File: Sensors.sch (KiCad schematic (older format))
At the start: 68 parts, among them CON1 CONSOLE, IC1 ATMEGA328P, P1 CONN_01X08, P10 GPIO, P11 I2C, P12 96B-GPIO, P13 96B-I2C0, P14 GPIO, P15 GPIO, P16 GPIO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

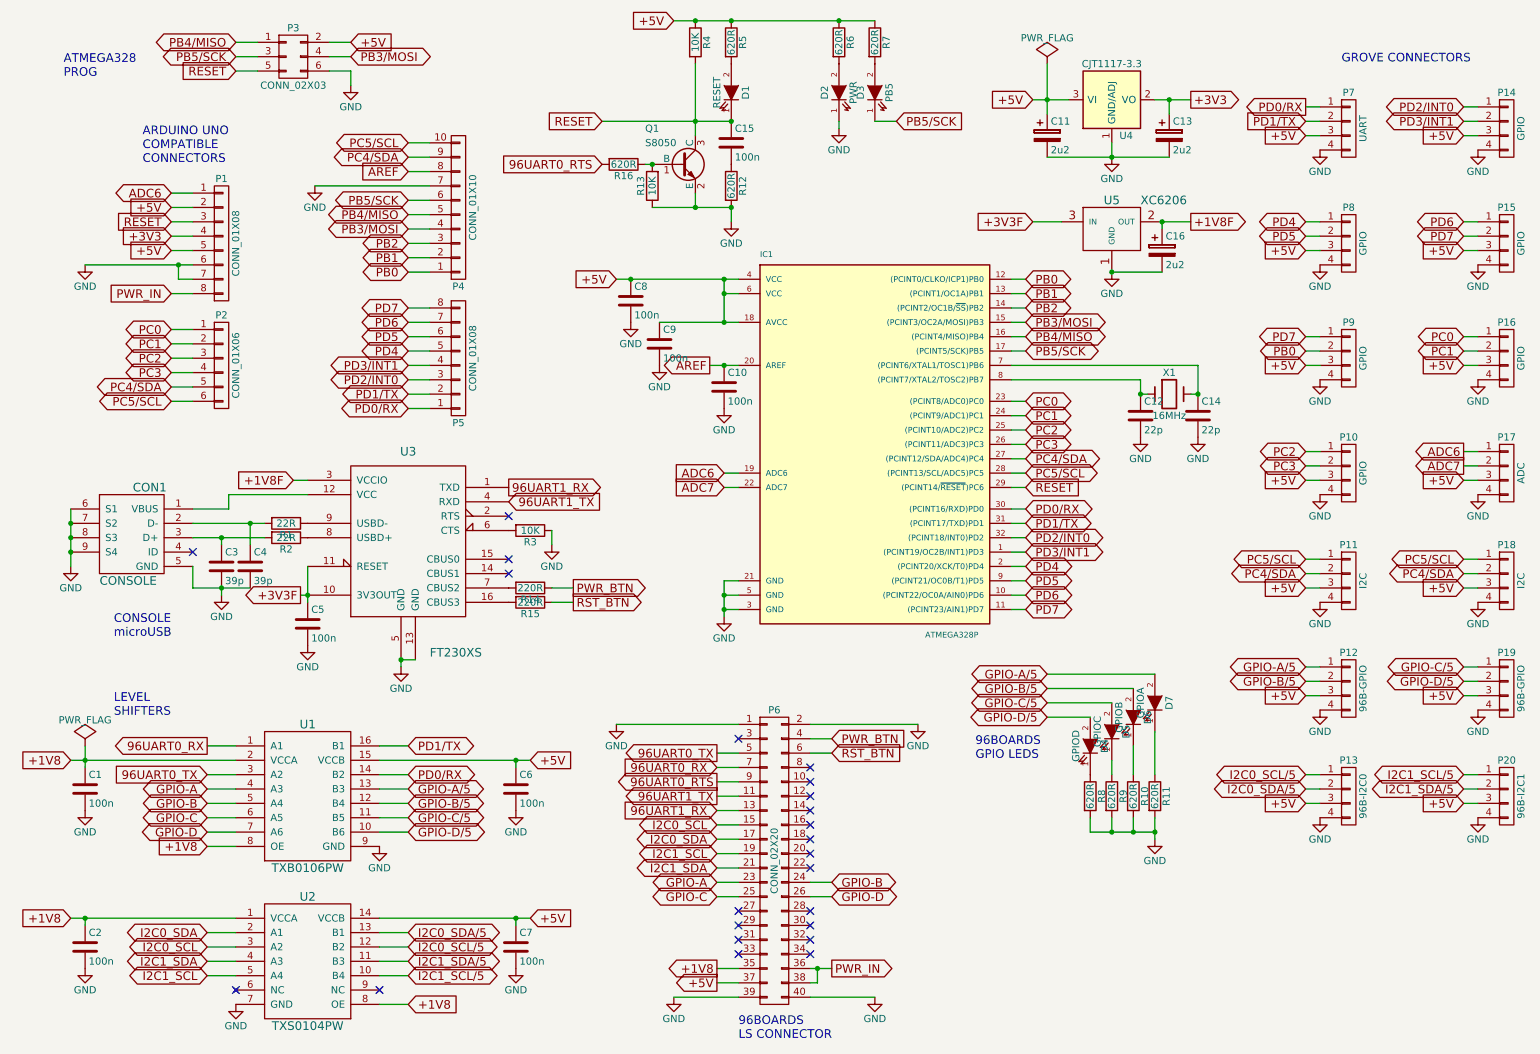
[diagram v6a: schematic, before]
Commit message: Rewire PB5 LED to drive high to light and use a 1K resistor
The first rev had the LED tied to +5V, and PB5 needed to pull it low to
light. This doesn't play well with USBTinyISP because it puts too much
load on the line for the programmer to actually program the Arduino, and
it is opposite to the way the led is wired on every other Arduino. Fix
it to be consistent with the rest of the Arduino world.

Signed-off-by: Grant Likely <grant.likely@linaro.org>
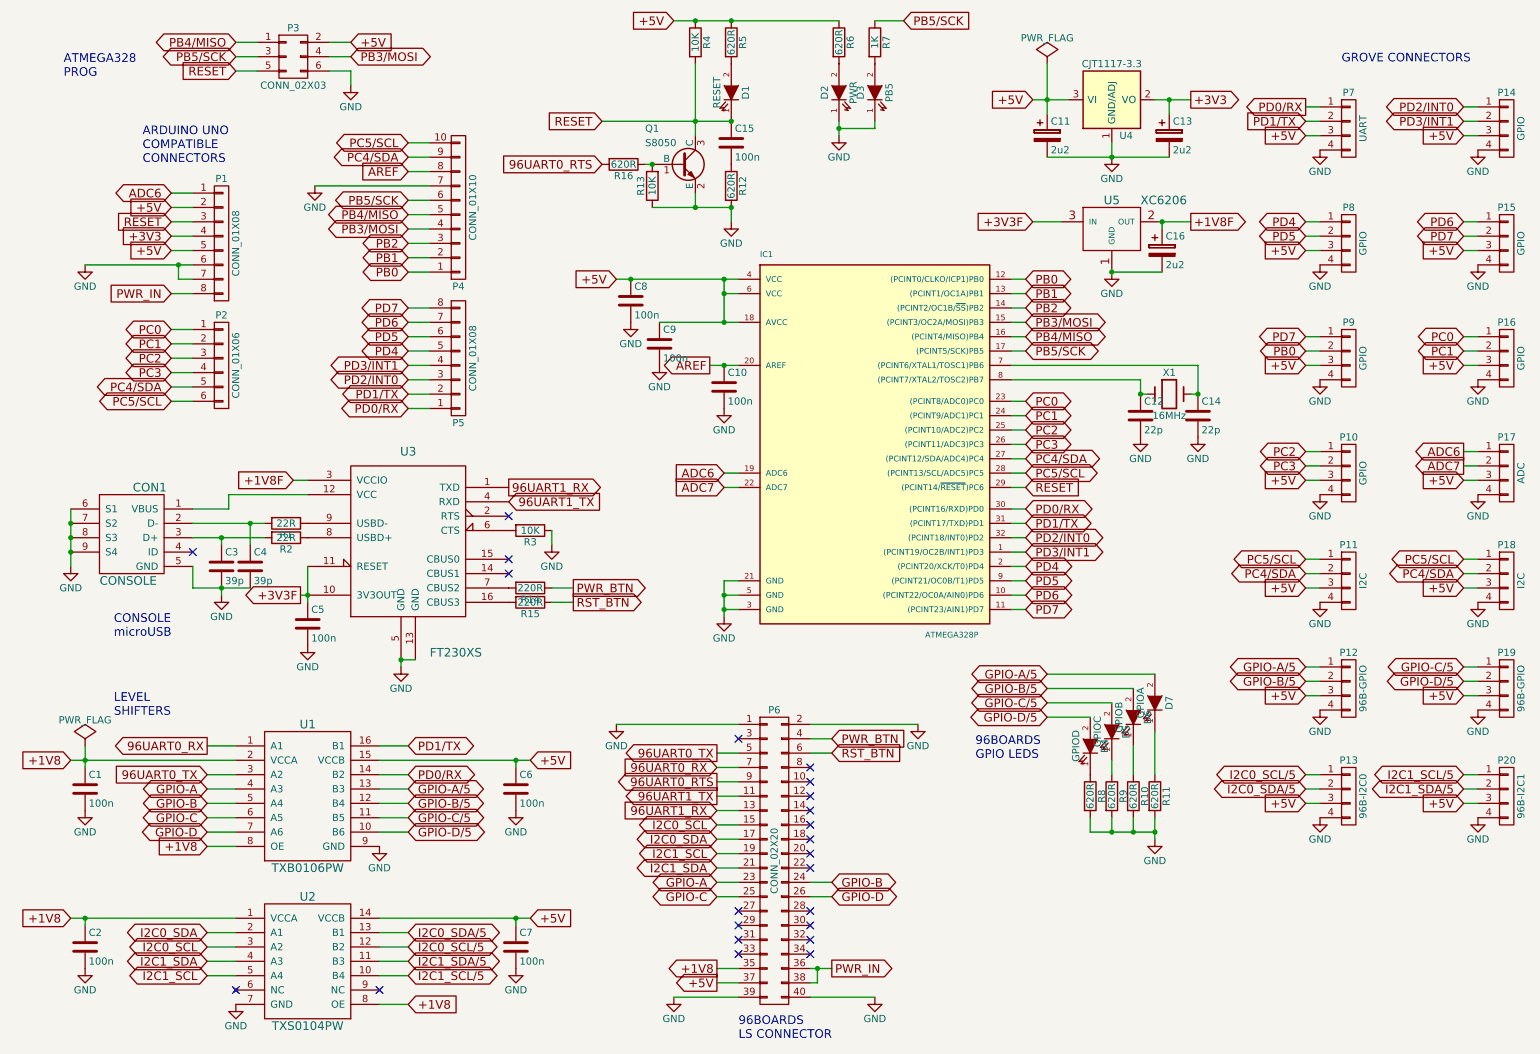
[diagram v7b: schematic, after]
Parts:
- R7: value 620R -> 1K
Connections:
- net +5V: no longer R7.1
- net GND: now also D3.1 (K)
- net PB5/SCK: now also R7.1; no longer D3.1 (K)
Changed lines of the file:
@@
 L GND #PWR030
 U 1 1 55BFA7BD
-P 6250 1350
-F 0 "#PWR030" H 6250 1100 50  0001 C CNN
-F 1 "GND" H 6250 1200 50  0000 C CNN
-F 2 "" H 6250 1350 60  0000 C CNN
-F 3 "" H 6250 1350 60  0000 C CNN
-	1    6250 1350
+P 6250 1400
+F 0 "#PWR030" H 6250 1150 50  0001 C CNN
+F 1 "GND" H 6250 1250 50  0000 C CNN
+F 2 "" H 6250 1400 60  0000 C CNN
+F 3 "" H 6250 1400 60  0000 C CNN
+	1    6250 1400
 	1    0    0    -1
 $EndComp
@@
 P 6500 750
 F 0 "R7" V 6580 750 50  0000 C CNN
-F 1 "620R" V 6500 750 50  0000 C CNN
+F 1 "1K" V 6500 750 50  0000 C CNN
 F 2 "Sensors:R_0603_Seeed" V 6430 750 30  0001 C CNN
 F 3 "" H 6500 750 30  0000 C CNN
@@
 	0    -1   -1   0
 $EndComp
-Text GLabel 6650 1300 2    60   Input ~ 0
+Text GLabel 6700 600  2    60   Input ~ 0
 PB5/SCK
 Text GLabel 5400 6000 0    60   Output ~ 0
@@
 	1750 3250 1600 3250
 Wire Wire Line
-	1000 2300 1650 2300
-Wire Wire Line
-	1650 2300 1750 2300
+	1000 2300 1750 2300
 Wire Wire Line
 	1750 2400 1650 2400
@@
 	7450 2900 7550 2900
 Wire Wire Line
-	4700 2400 4800 2400
-Wire Wire Line
-	4800 2400 5450 2400
-Wire Wire Line
-	5450 2400 5550 2400
+	4700 2400 5550 2400
 Wire Wire Line
 	5550 2500 5450 2500
 Wire Wire Line
-	5450 2400 5450 2500
-Wire Wire Line
-	5450 2500 5450 2700
+	5450 2400 5450 2700
 Connection ~ 5450 2400
 Connection ~ 4800 2400
 Wire Wire Line
-	5000 2700 5450 2700
-Wire Wire Line
-	5450 2700 5550 2700
-Wire Wire Line
-	5350 3000 5450 3000
-Wire Wire Line
-	5450 3000 5550 3000
+	5000 2700 5550 2700
+Wire Wire Line
+	5350 3000 5550 3000
 Wire Wire Line
 	7450 3000 8750 3000
@@
 	5550 4500 5450 4500
 Wire Wire Line
-	5450 4500 5450 4600
-Wire Wire Line
-	5450 4600 5450 4700
-Wire Wire Line
-	5450 4700 5450 4750
+	5450 4500 5450 4750
 Wire Wire Line
 	5450 4700 5550 4700
@@
 	5400 5800 5550 5800
 Wire Wire Line
-	8450 1150 8550 1150
-Wire Wire Line
-	8550 1150 8700 1150
-Wire Wire Line
-	7700 1550 8150 1550
-Wire Wire Line
-	8150 1550 8550 1550
+	8450 1150 8700 1150
+Wire Wire Line
+	7700 1550 8550 1550
 Wire Wire Line
 	8550 1250 8550 1150
@@
 Connection ~ 5500 600
 Wire Wire Line
-	4600 1300 5250 1300
-Wire Wire Line
-	5250 1300 5500 1300
+	4600 1300 5500 1300
 Connection ~ 5250 1300
 Connection ~ 5500 1300
 Wire Wire Line
-	5100 600  5250 600
-Wire Wire Line
-	5250 600  5500 600
-Wire Wire Line
-	5500 600  6250 600
-Wire Wire Line
-	6250 600  6500 600
+	5100 600  6250 600
 Wire Wire Line
 	1850 5650 2050 5650
 Wire Wire Line
-	900  5750 1000 5750
-Wire Wire Line
-	1000 5750 2050 5750
+	900  5750 2050 5750
 Connection ~ 1000 5750
 Wire Wire Line
-	1000 5650 1000 5750
-Wire Wire Line
-	1000 5750 1000 5800
+	1000 5650 1000 5800
 Wire Wire Line
 	3050 5650 3250 5650
 Wire Wire Line
-	3050 5750 4000 5750
-Wire Wire Line
-	4000 5750 4100 5750
+	3050 5750 4100 5750
 Connection ~ 4000 5750
 Wire Wire Line
@@
 	3250 7450 3050 7450
 Wire Wire Line
-	900  6850 1000 6850
-Wire Wire Line
-	1000 6850 2050 6850
+	900  6850 2050 6850
 Wire Wire Line
 	1000 6900 1000 6850
@@
 	5550 5500 4700 5500
 Wire Wire Line
-	3050 6850 4000 6850
-Wire Wire Line
-	4000 6850 4100 6850
+	3050 6850 4100 6850
 Wire Wire Line
 	4000 6900 4000 6850
@@
 	8150 5750 8150 5850
 Wire Wire Line
-	8000 6250 8150 6250
-Wire Wire Line
-	8150 6250 8300 6250
-Wire Wire Line
-	8300 6250 8450 6250
-Wire Wire Line
-	8450 6150 8450 6250
-Wire Wire Line
-	8450 6250 8450 6300
+	8000 6250 8450 6250
+Wire Wire Line
+	8450 6150 8450 6300
 Wire Wire Line
 	8000 6150 8000 6250
@@
 Connection ~ 8150 1550
 Wire Wire Line
-	7700 900  7700 1150
-Wire Wire Line
-	7700 1150 7700 1250
+	7700 900  7700 1250
 Connection ~ 7700 1150
-Connection ~ 6250 600
-Wire Wire Line
-	6650 1300 6500 1300
 Wire Wire Line
 	5400 6000 5550 6000
@@
 	5400 6100 5550 6100
 Wire Wire Line
-	900  4000 900  4100
-Wire Wire Line
-	900  4100 900  4200
-Wire Wire Line
-	900  4200 900  4300
-Wire Wire Line
-	900  4300 900  4400
+	900  4000 900  4400
 Connection ~ 900  4100
 Connection ~ 900  4200
 Connection ~ 900  4300
 Wire Wire Line
-	1750 4100 2150 4100
-Wire Wire Line
-	2150 4100 2250 4100
-Wire Wire Line
-	1750 4200 1950 4200
-Wire Wire Line
-	1950 4200 2250 4200
+	1750 4100 2250 4100
+Wire Wire Line
+	1750 4200 2250 4200
 Wire Wire Line
 	2150 4250 2150 4100
@@
 	1750 4400 1750 4550
 Wire Wire Line
-	1750 4550 1950 4550
-Wire Wire Line
-	1950 4550 2150 4550
+	1750 4550 2150 4550
 Connection ~ 1950 4550
 Wire Wire Line
@@
 	2000 3900 2550 3900
 Wire Wire Line
-	2550 4400 2550 4600
-Wire Wire Line
-	2550 4600 2550 4650
+	2550 4400 2550 4650
 Connection ~ 2550 4600
 Wire Wire Line
@@
 	6100 7300 6100 7200
 Wire Wire Line
-	6050 7200 6100 7200
-Wire Wire Line
-	6100 7200 6200 7200
+	6050 7200 6200 7200
 Connection ~ 6100 7200
 NoConn ~ 1750 4300
@@
 	8500 2050 8500 2000
 Wire Wire Line
-	7600 1150 7700 1150
-Wire Wire Line
-	7700 1150 7850 1150
+	7600 1150 7850 1150
 Text GLabel 2500 4600 0    60   Output ~ 0
 +3V3F
@@
 $EndComp
 Wire Wire Line
-	4950 1900 5250 1900
-Wire Wire Line
-	5250 1900 5500 1900
+	4950 1900 5500 1900
 Connection ~ 5500 1900
 Wire Wire Line
-	5250 900  5250 1300
-Wire Wire Line
-	5250 1300 5250 1400
+	5250 900  5250 1400
 $Comp
 L R R16
@@
 Connection ~ 5250 1900
 Wire Wire Line
-	6250 1350 6250 1300
+	6250 1300 6250 1400
+Wire Wire Line
+	6250 1350 6500 1350
+Wire Wire Line
+	6500 1350 6500 1300
+Connection ~ 6250 1350
+Wire Wire Line
+	6500 600  6700 600
 $EndSCHEMATC

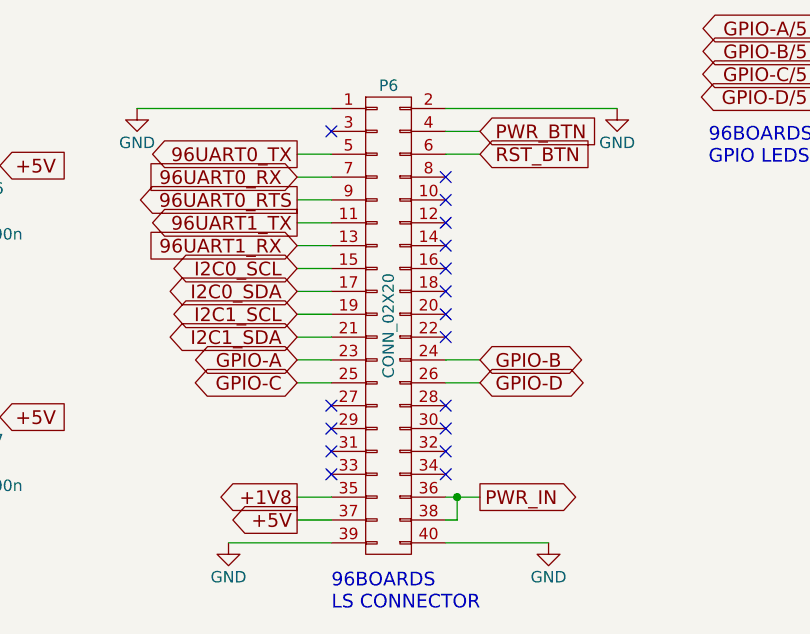
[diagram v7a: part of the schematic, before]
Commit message: Add labels for SPI and all the GPIOs
No functional change, just put the labels in so that they can be used in
a later change.

Signed-off-by: Grant Likely <grant.likely@linaro.org>
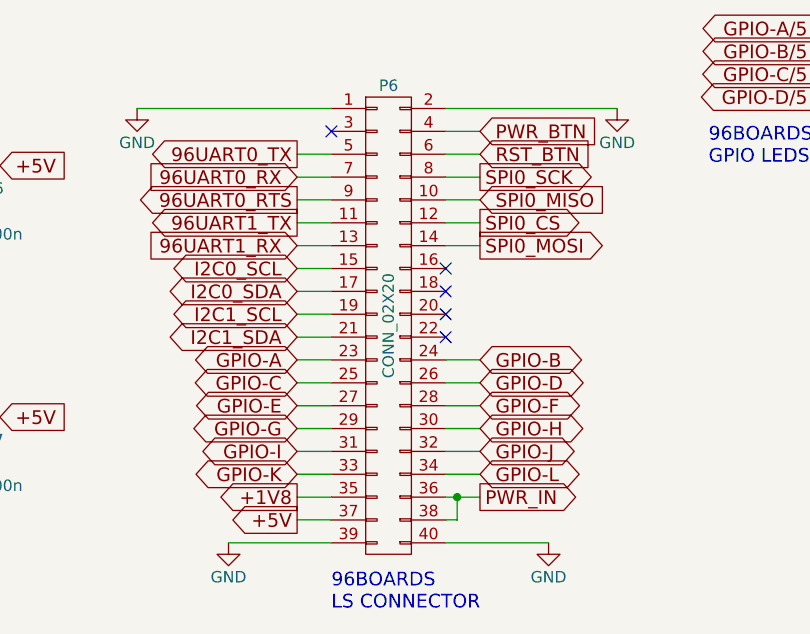
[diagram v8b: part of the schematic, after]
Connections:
- net SPI0_MISO: now reaches P6.10 (P10)
- net SPI0_CS: now reaches P6.12 (P12)
- net SPI0_MOSI: now reaches P6.14 (P14)
- net GPIO-E: now reaches P6.27 (P27)
- net GPIO-F: now reaches P6.28 (P28)
- net GPIO-G: now reaches P6.29 (P29)
- net GPIO-H: now reaches P6.30 (P30)
- net GPIO-I: now reaches P6.31 (P31)
- net GPIO-J: now reaches P6.32 (P32)
- net GPIO-K: now reaches P6.33 (P33)
- net GPIO-L: now reaches P6.34 (P34)
- net SPI0_SCK: now reaches P6.8 (P8)
- no-connect marks 23 -> 11
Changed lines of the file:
@@
 NoConn ~ 2050 7350
 NoConn ~ 5550 5600
-NoConn ~ 5550 6900
-NoConn ~ 5550 7000
-NoConn ~ 5550 7100
-NoConn ~ 6050 5800
-NoConn ~ 6050 5900
-NoConn ~ 6050 6000
-NoConn ~ 6050 6100
 NoConn ~ 6050 6200
 NoConn ~ 6050 6300
 NoConn ~ 6050 6400
 NoConn ~ 6050 6500
-NoConn ~ 6050 6800
-NoConn ~ 6050 6900
-NoConn ~ 6050 7000
-NoConn ~ 6050 7100
 Wire Wire Line
 	10600 4550 10700 4550
@@
 Wire Wire Line
 	5550 5900 5400 5900
-NoConn ~ 5550 6800
 $Comp
 L BC817-40 Q1
@@
 Wire Wire Line
 	6500 600  6700 600
+Text GLabel 6200 5800 2    60   Output ~ 0
+SPI0_SCK
+Text GLabel 6200 5900 2    60   Input ~ 0
+SPI0_MISO
+Text GLabel 6200 6000 2    60   Output ~ 0
+SPI0_CS
+Text GLabel 6200 6100 2    60   Output ~ 0
+SPI0_MOSI
+Wire Wire Line
+	6050 5800 6200 5800
+Wire Wire Line
+	6050 5900 6200 5900
+Wire Wire Line
+	6050 6000 6200 6000
+Wire Wire Line
+	6050 6100 6200 6100
+Text GLabel 6200 6800 2    60   BiDi ~ 0
+GPIO-F
+Text GLabel 6200 6900 2    60   BiDi ~ 0
+GPIO-H
+Text GLabel 6200 7000 2    60   BiDi ~ 0
+GPIO-J
+Text GLabel 6200 7100 2    60   BiDi ~ 0
+GPIO-L
+Wire Wire Line
+	6050 6800 6200 6800
+Wire Wire Line
+	6050 6900 6200 6900
+Wire Wire Line
+	6050 7000 6200 7000
+Wire Wire Line
+	6050 7100 6200 7100
+Text GLabel 5400 6800 0    60   BiDi ~ 0
+GPIO-E
+Text GLabel 5400 6900 0    60   BiDi ~ 0
+GPIO-G
+Text GLabel 5400 7000 0    60   BiDi ~ 0
+GPIO-I
+Text GLabel 5400 7100 0    60   BiDi ~ 0
+GPIO-K
+Wire Wire Line
+	5400 6800 5550 6800
+Wire Wire Line
+	5400 6900 5550 6900
+Wire Wire Line
+	5400 7000 5550 7000
+Wire Wire Line
+	5400 7100 5550 7100
 $EndSCHEMATC
